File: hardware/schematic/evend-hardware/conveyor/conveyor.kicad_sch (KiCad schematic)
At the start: 66 parts, among them M2 Stepper_Motor_unipolar_6pin, Q1 Q_NPN_BEC, U1 LM393, X1 Conn_01x06, X2 MDB, X3 Conn_01x06

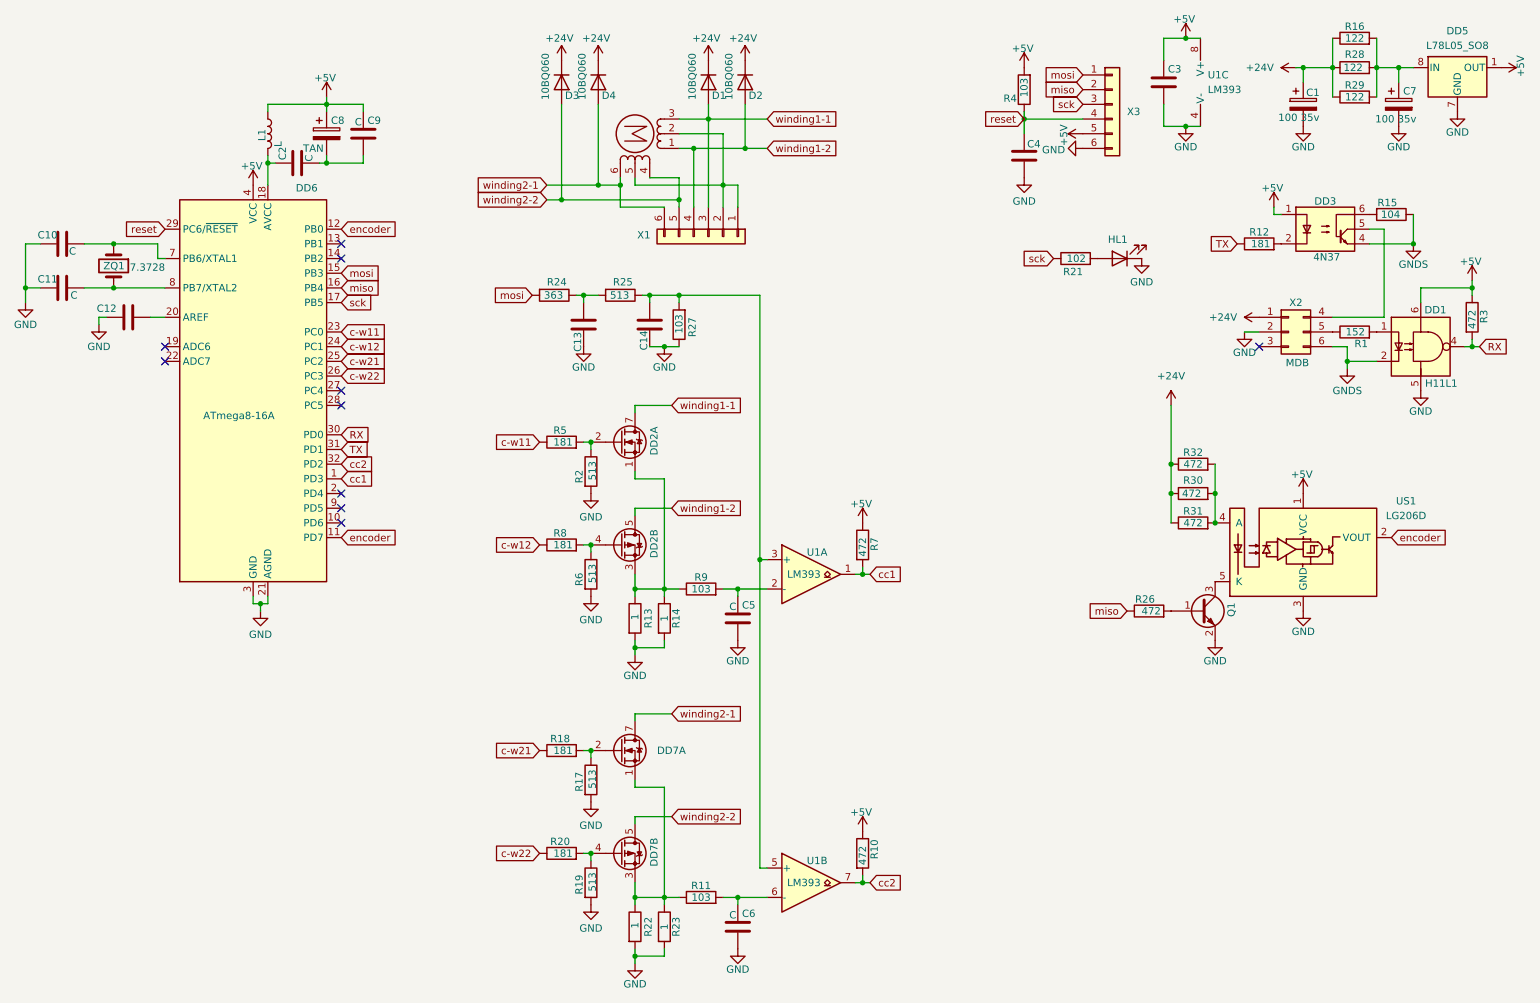
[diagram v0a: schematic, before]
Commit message: update conveyor schematic
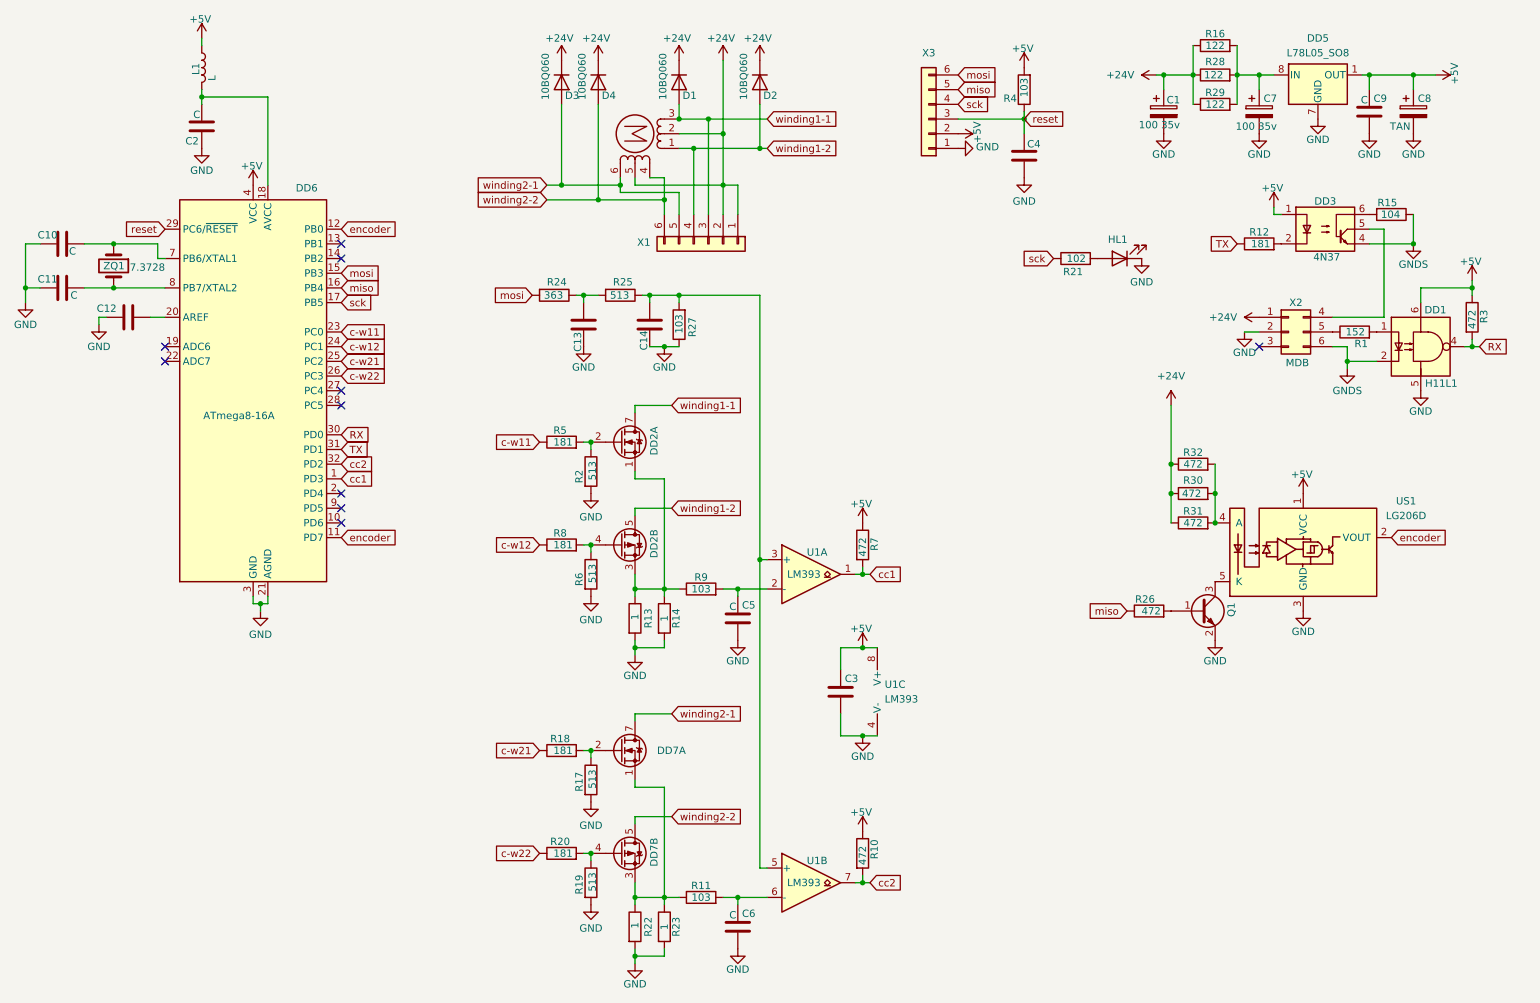
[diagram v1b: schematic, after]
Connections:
- net +24V: now also M2.2, M2.5, X1.1 (Pin_1), X1.2 (Pin_2)
- net +5V: now also X3.2 (Pin_2); no longer X3.5 (Pin_5)
- net GND: now also C2.1, C8.2, C9.1, X3.1 (Pin_1); no longer X3.6 (Pin_6)
- net miso: now also X3.5 (Pin_5); no longer X3.2 (Pin_2)
- net mosi: now also X3.6 (Pin_6); no longer X3.1 (Pin_1)
- net reset: now also X3.3 (Pin_3); no longer X3.4 (Pin_4)
- net sck: now also X3.4 (Pin_4); no longer X3.3 (Pin_3)
- net winding2-1: now also D3.2 (A), X1.5 (Pin_5); no longer D4.2 (A), X1.6 (Pin_6)
- net winding2-2: now also D4.2 (A), X1.6 (Pin_6); no longer D3.2 (A), X1.5 (Pin_5)
- net at DD6.18 (AVCC), L1.2: now also C2.2; no longer C2.1
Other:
- moved on the sheet: C1, C2, C3, C7, C8, C9, D1, D2, DD5, L1, R16, R28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
